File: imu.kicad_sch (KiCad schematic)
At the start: 33 parts, among them J1 USB_C_Receptacle_USB2.0_16P, SW1 SW_Push, SW2 SW_Push, U1 LSM6DSL, U2 LIS2MDL, U3 AMS1117-3.3, U4 ESP32-C3-WROOM-02

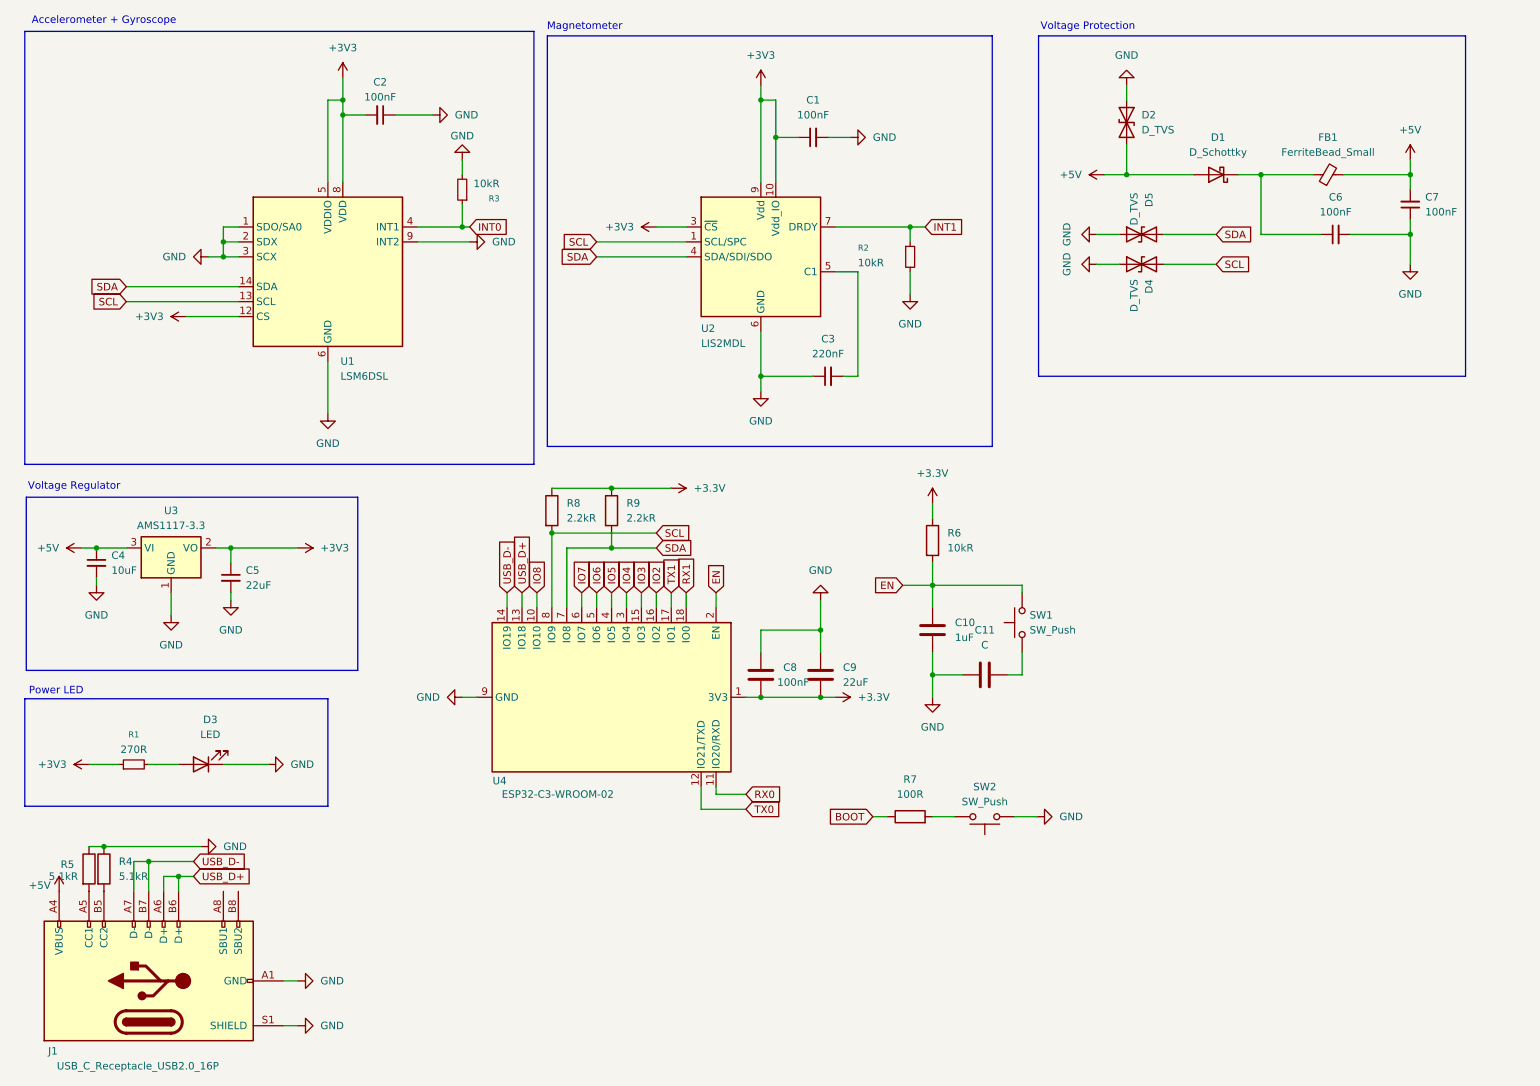
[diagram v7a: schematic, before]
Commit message: Add Hierarchal Schematic + JST Connectors + GPIO
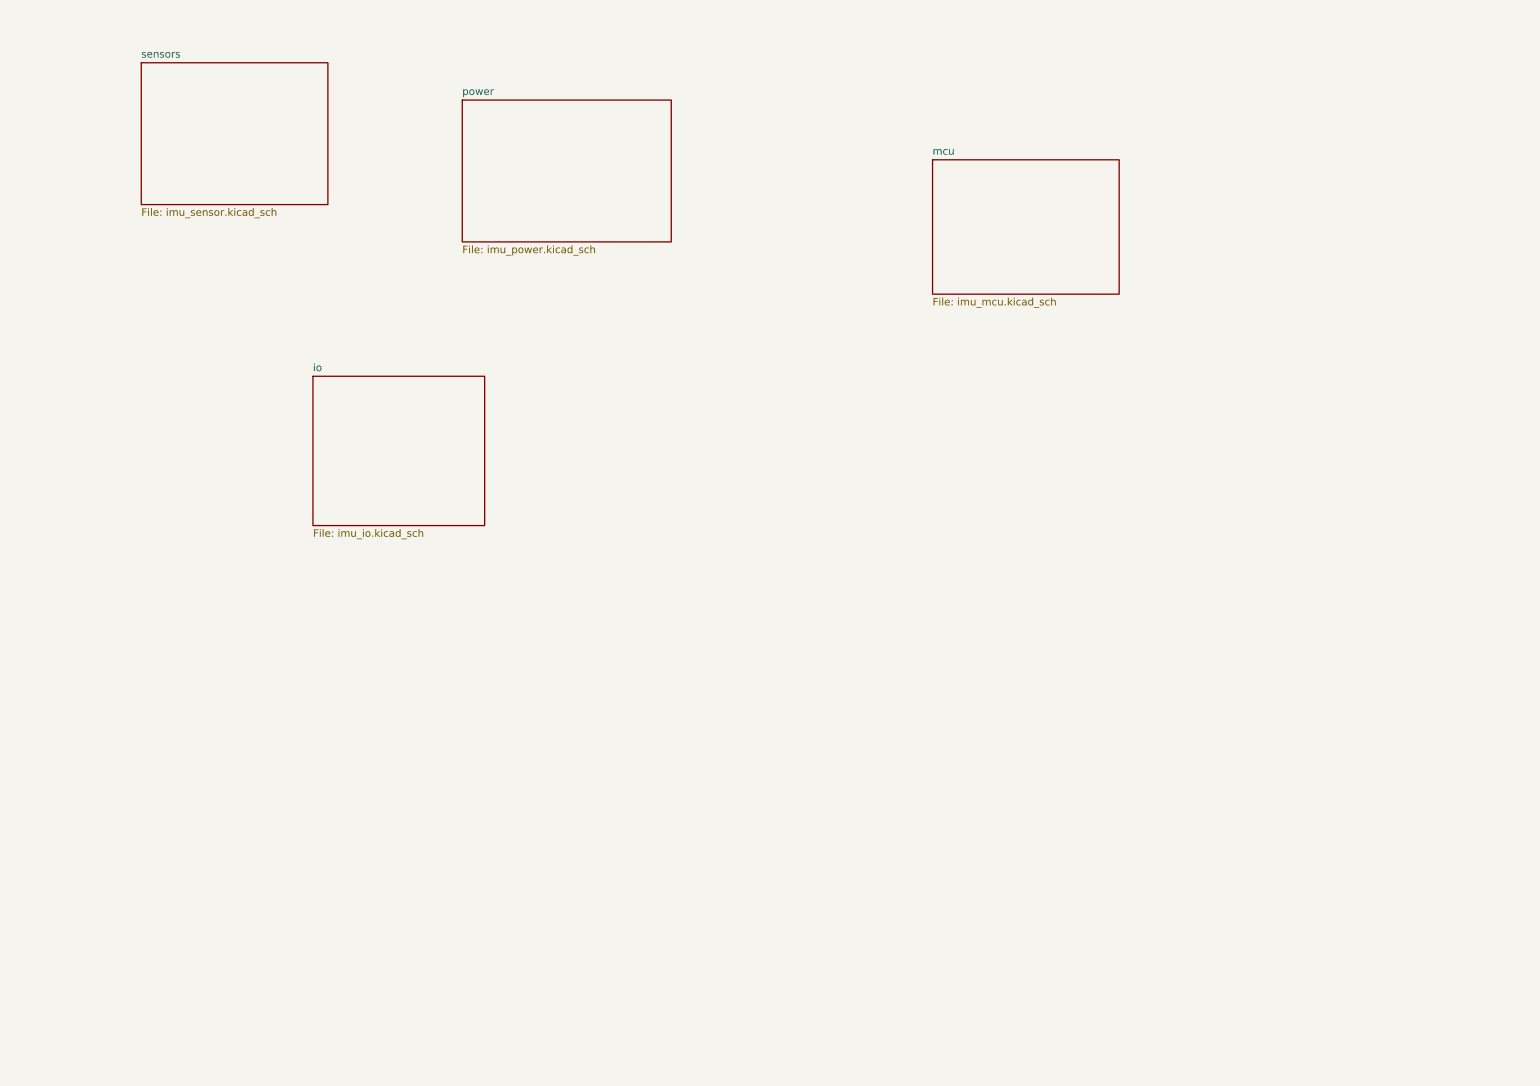
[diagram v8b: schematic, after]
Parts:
- removed C1, C2, C6, C7: 100nF, Capacitor_SMD:C_0805_2012Metric_Pad1.18x1.45mm_HandSolder, symbol Device:C_Small
- removed C10: 1uF, symbol Device:C
- removed C11: C, symbol Device:C
- removed C3: 220nF, Capacitor_SMD:C_0805_2012Metric_Pad1.18x1.45mm_HandSolder, symbol Device:C_Small
- removed C4: 10uF, Capacitor_SMD:C_0805_2012Metric_Pad1.18x1.45mm_HandSolder, symbol Device:C_Small
- removed C5: 22uF, Capacitor_SMD:C_0805_2012Metric_Pad1.18x1.45mm_HandSolder, symbol Device:C_Small
- removed C8: 100nF, symbol Device:C
- removed C9: 22uF, symbol Device:C
- removed D1: D_Schottky, Diode_SMD:D_SOD-123F, symbol Device:D_Schottky
- removed D2: D_TVS, Diode_SMD:D_SMB, symbol Device:D_TVS
- removed D3: LED, LED_SMD:LED_0805_2012Metric_Pad1.15x1.40mm_HandSolder, symbol Device:LED
- removed D4, D5: D_TVS, Diode_SMD:D_SOD-323_HandSoldering, symbol Device:D_TVS
- removed FB1: FerriteBead_Small, Inductor_SMD:L_0805_2012Metric_Pad1.05x1.20mm_HandSolder, symbol Device:FerriteBead_Small
- removed J1: USB_C_Receptacle_USB2.0_16P, symbol Connector:USB_C_Receptacle_USB2.0_16P
- removed R1: 270R, Resistor_SMD:R_0805_2012Metric_Pad1.20x1.40mm_HandSolder, symbol Device:R_Small
- removed R2, R3: 10kR, Resistor_SMD:R_0805_2012Metric_Pad1.20x1.40mm_HandSolder, symbol Device:R_Small
- removed R4, R5: 5.1kR, symbol Device:R
- removed R6: 10kR, symbol Device:R
- removed R7: 100R, symbol Device:R
- removed R8, R9: 2.2kR, symbol Device:R
- removed SW1, SW2: SW_Push, symbol Switch:SW_Push
- removed U1: LSM6DSL, Package_LGA:LGA-14_3x2.5mm_P0.5mm_LayoutBorder3x4y, symbol Sensor_Motion:LSM6DSL
- removed U2: LIS2MDL, Package_LGA:LGA-12_2x2mm_P0.5mm, symbol Sensor_Magnetic:LIS2MDL
- removed U3: AMS1117-3.3, Package_TO_SOT_SMD:SOT-223-3_TabPin2, symbol Regulator_Linear:AMS1117-3.3
- removed U4: ESP32-C3-WROOM-02, RF_Module:ESP32-C3-WROOM-02, symbol RF_Module:ESP32-C3-WROOM-02
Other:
- added sheet io (imu_io.kicad_sch)
- added sheet mcu (imu_mcu.kicad_sch)
- added sheet power (imu_power.kicad_sch)
- added sheet sensors (imu_sensor.kicad_sch)
- note removed: "Accelerometer + Gyroscope"
- note removed: "Magnetometer"
- note removed: "Power LED"
- note removed: "Voltage Protection"
- note removed: "Voltage Regulator"
